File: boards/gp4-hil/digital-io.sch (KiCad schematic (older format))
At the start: 15 parts, among them Q1 SSM6N58NU, U15 TS3A4751, U16 TS3A4751, U17 TS3A4751, U18 TS3A4751, U19 TS3A4751, U2 XC7A100T-1FTG256C

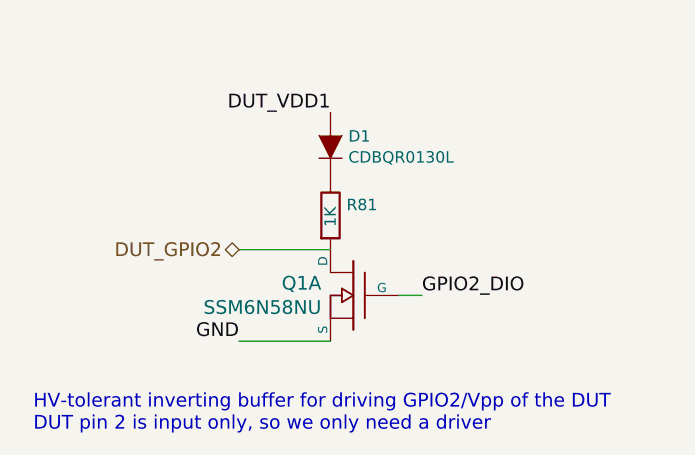
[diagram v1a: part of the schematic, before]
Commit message: Continued work on test board. Finally hooked up remote sense for 1V0.
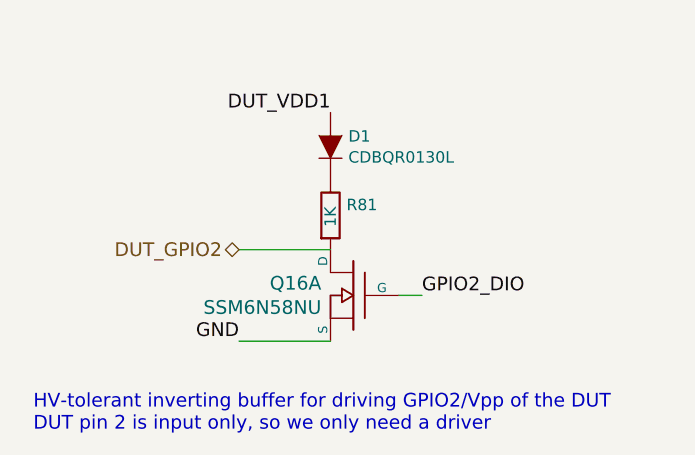
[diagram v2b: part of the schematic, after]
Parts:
- renumbered Q1 to Q16
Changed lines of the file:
@@
 Sheet 7 7
 Title "GreenPak Hardware-In-Loop Test Platform"
-Date "2016-06-05"
+Date "2016-06-10"
 Rev "0.1"
 Comp "Andrew Zonenberg"
@@
 HV-tolerant inverting buffer for driving GPIO2/Vpp of the DUT\nDUT pin 2 is input only, so we only need a driver
 $Comp
-L SSM6N58NU_DUAL_NMOS Q1
+L SSM6N58NU_DUAL_NMOS Q16
 U 1 1 573D1681
 P 2250 11150
-F 0 "Q1" H 2390 11203 60  0000 L CNN
+F 0 "Q16" H 2390 11203 60  0000 L CNN
 F 1 "SSM6N58NU" H 2390 11097 60  0000 L CNN
 F 2 "azonenberg_pcb:DFN_6_0.65MM_2x2MM_GDS" H 2250 11150 60  0001 C CNN

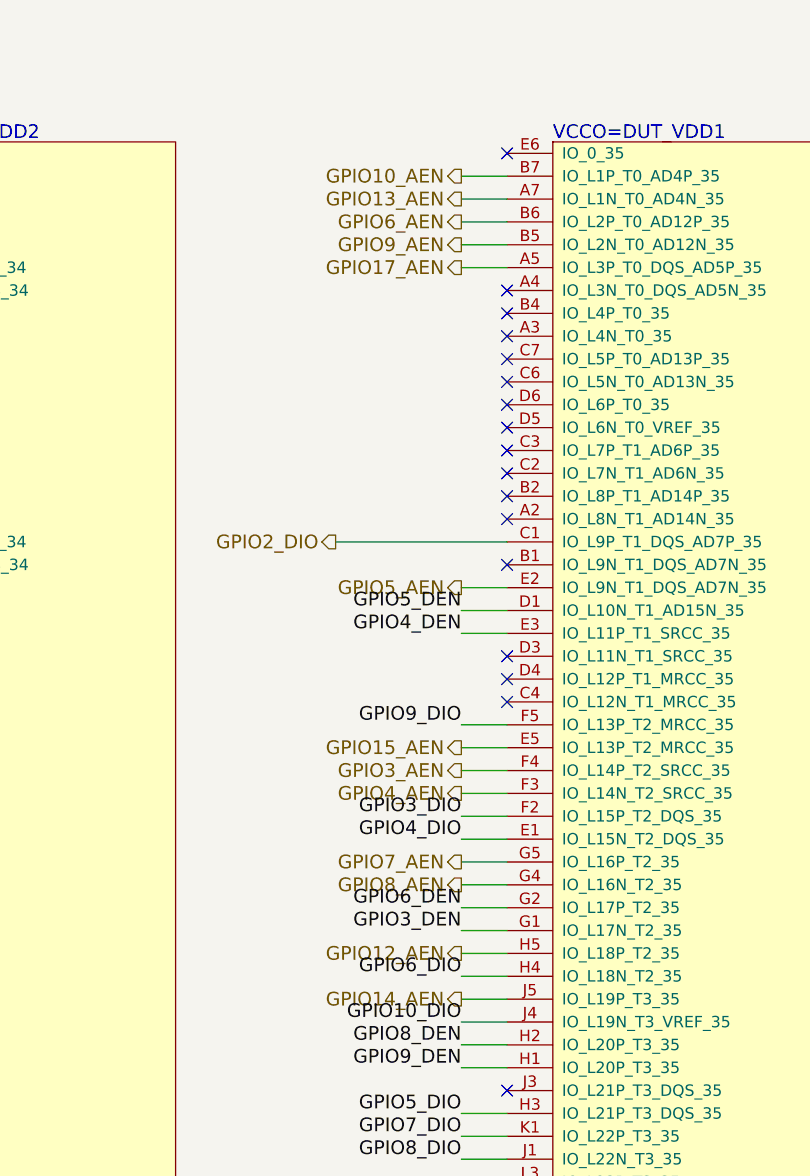
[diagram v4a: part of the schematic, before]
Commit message: Continued routing, began DAC stuff
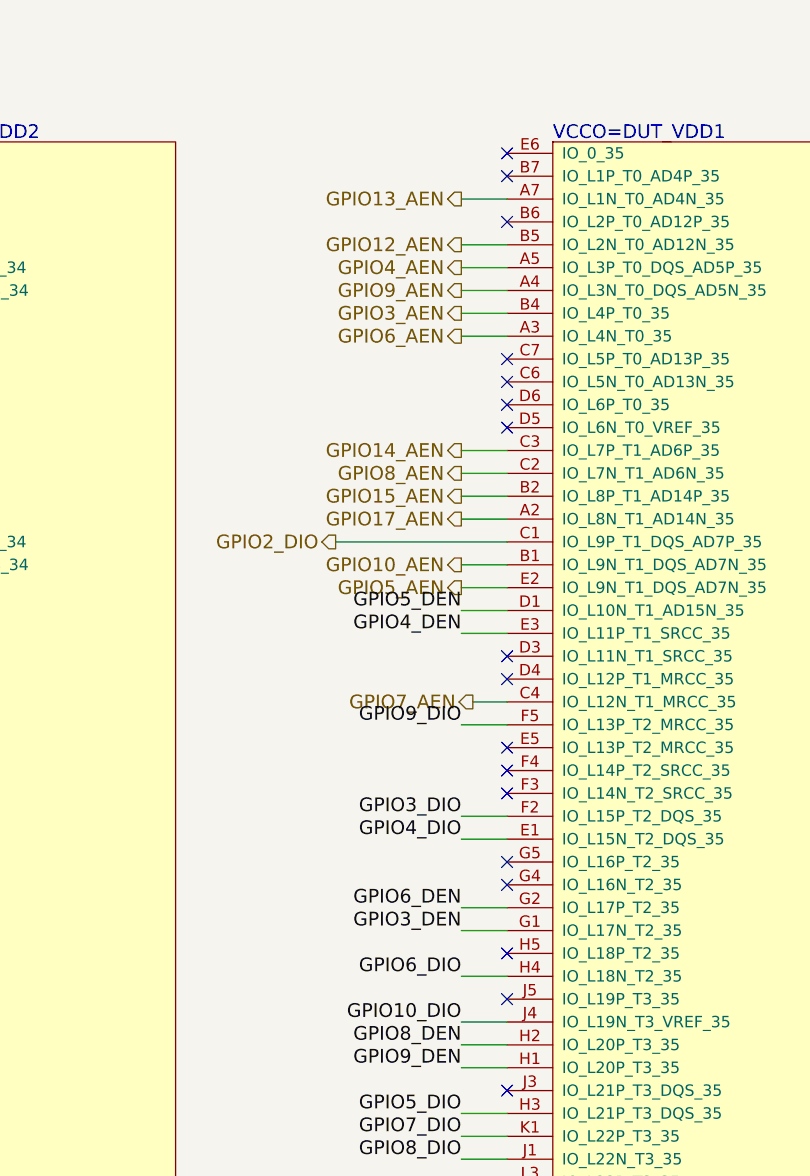
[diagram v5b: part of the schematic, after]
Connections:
- net GPIO10_AEN: now also U2.B1 (IO_L9N_T1_DQS_AD7N_35); no longer U2.B7 (IO_L1P_T0_AD4P_35)
- net GPIO12_AEN: now also U2.B5 (IO_L2N_T0_AD12N_35); no longer U2.H5 (IO_L18P_T2_35)
- net GPIO14_AEN: now also U2.C3 (IO_L7P_T1_AD6P_35); no longer U2.J5 (IO_L19P_T3_35)
- net GPIO15_AEN: now also U2.B2 (IO_L8P_T1_AD14P_35); no longer U2.E5 (IO_L13P_T2_MRCC_35)
- net GPIO17_AEN: now also U2.A2 (IO_L8N_T1_AD14N_35); no longer U2.A5 (IO_L3P_T0_DQS_AD5P_35)
- net GPIO3_AEN: now also U2.B4 (IO_L4P_T0_35); no longer U2.F4 (IO_L14P_T2_SRCC_35)
- net GPIO4_AEN: now also U2.A5 (IO_L3P_T0_DQS_AD5P_35); no longer U2.F3 (IO_L14N_T2_SRCC_35)
- net GPIO6_AEN: now also U2.A3 (IO_L4N_T0_35); no longer U2.B6 (IO_L2P_T0_AD12P_35)
- net GPIO7_AEN: now also U2.C4 (IO_L12N_T1_MRCC_35); no longer U2.G5 (IO_L16P_T2_35)
- net GPIO8_AEN: now also U2.C2 (IO_L7N_T1_AD6N_35); no longer U2.G4 (IO_L16N_T2_35)
- net GPIO9_AEN: now also U2.A4 (IO_L3N_T0_DQS_AD5N_35); no longer U2.B5 (IO_L2N_T0_AD12N_35)
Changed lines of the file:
@@
 Sheet 7 7
 Title "GreenPak Hardware-In-Loop Test Platform"
-Date "2016-06-12"
+Date "2016-06-13"
 Rev "0.1"
 Comp "Andrew Zonenberg"
@@
 Text HLabel 1500 8800 0    60   BiDi ~ 0
 DUT_GPIO20
-$Comp
-L XC7AxT-xFTG256x U?
-U 6 1 573B2D61
-P 19350 7550
-AR Path="/57316B0C/573B2D61" Ref="U?"  Part="1"
-AR Path="/573AABB3/573B2D61" Ref="U2"  Part="6"
-F 0 "U2" H 19350 7350 60  0000 L CNN
-F 1 "XC7A100T-1FTG256C" H 19350 7450 60  0000 L CNN
-F 2 "azonenberg_pcb:BGA_256_17x17_FULLARRAY_1MM" H 19350 7550 60  0001 C CNN
-F 3 "" H 19350 7550 60  0000 C CNN
-	6    19350 7550
-	1    0    0    -1
-$EndComp
 $Comp
 L TS3A4751 U15
@@
 	16150 3550 16000 3550
 Wire Wire Line
-	19150 2750 18950 2750
+	19150 4450 18950 4450
 Wire Wire Line
 	18950 2850 19150 2850
 Wire Wire Line
-	19150 2950 18950 2950
-Wire Wire Line
-	18950 3050 19150 3050
-Wire Wire Line
-	19150 3150 18950 3150
+	19150 3450 18950 3450
+Wire Wire Line
+	18950 3250 19150 3250
+Wire Wire Line
+	19150 4250 18950 4250
 Wire Wire Line
 	18950 7050 19150 7050
@@
 	19150 5150 18950 5150
 Wire Wire Line
-	18950 5250 19150 5250
+	18950 4150 19150 4150
 Wire Wire Line
 	7500 1300 7700 1300
@@
 	1750 11350 2150 11350
 NoConn ~ 19150 2650
-Text HLabel 18950 5350 0    60   Output ~ 0
+Text HLabel 18950 3350 0    60   Output ~ 0
 GPIO3_AEN
-Text HLabel 18950 5450 0    60   Output ~ 0
+Text HLabel 18950 3150 0    60   Output ~ 0
 GPIO4_AEN
 Text HLabel 18950 4550 0    60   Output ~ 0
 GPIO5_AEN
-Text HLabel 18950 2950 0    60   Output ~ 0
+Text HLabel 18950 3450 0    60   Output ~ 0
 GPIO6_AEN
-Text HLabel 18950 5750 0    60   Output ~ 0
+Text HLabel 19000 5050 0    60   Output ~ 0
 GPIO7_AEN
-Text HLabel 18950 5850 0    60   Output ~ 0
+Text HLabel 18950 4050 0    60   Output ~ 0
 GPIO8_AEN
+Text HLabel 18950 3250 0    60   Output ~ 0
+GPIO9_AEN
+Text HLabel 18950 4450 0    60   Output ~ 0
+GPIO10_AEN
+Wire Wire Line
+	18950 3350 19150 3350
+Wire Wire Line
+	19150 3150 18950 3150
+Wire Wire Line
+	18950 5550 19150 5550
+Wire Wire Line
+	19150 5650 18950 5650
+Wire Wire Line
+	19150 4050 18950 4050
+Wire Wire Line
+	18950 5950 19150 5950
+Wire Wire Line
+	19150 6050 18950 6050
 Text HLabel 18950 3050 0    60   Output ~ 0
-GPIO9_AEN
-Text HLabel 18950 2750 0    60   Output ~ 0
-GPIO10_AEN
-Wire Wire Line
-	18950 5350 19150 5350
-Wire Wire Line
-	19150 5450 18950 5450
-Wire Wire Line
-	18950 5550 19150 5550
-Wire Wire Line
-	19150 5650 18950 5650
-Wire Wire Line
-	18950 5750 19150 5750
-Wire Wire Line
-	19150 5850 18950 5850
-Wire Wire Line
-	18950 5950 19150 5950
-Wire Wire Line
-	19150 6050 18950 6050
-Text HLabel 18950 6150 0    60   Output ~ 0
 GPIO12_AEN
 Text HLabel 18950 2850 0    60   Output ~ 0
 GPIO13_AEN
-Text HLabel 18950 6350 0    60   Output ~ 0
+Text HLabel 18950 3950 0    60   Output ~ 0
 GPIO14_AEN
-Text HLabel 18950 5250 0    60   Output ~ 0
+Text HLabel 18950 4150 0    60   Output ~ 0
 GPIO15_AEN
-Text HLabel 18950 3150 0    60   Output ~ 0
+Text HLabel 18950 4250 0    60   Output ~ 0
 GPIO17_AEN
 Wire Wire Line
-	19150 6150 18950 6150
+	19150 3050 18950 3050
 Wire Wire Line
 	18950 6250 19150 6250
 Wire Wire Line
-	19150 6350 18950 6350
+	19150 3950 18950 3950
 Wire Wire Line
 	18950 6450 19150 6450
@@
 NoConn ~ 19150 3750
 NoConn ~ 19150 3850
-NoConn ~ 19150 3950
-NoConn ~ 19150 4050
-NoConn ~ 19150 4150
-NoConn ~ 19150 4250
 $Comp
 L XC7AxT-xFTG256x U?
@@
 Wire Wire Line
 	19150 7250 18950 7250
-NoConn ~ 19150 3450
 NoConn ~ 19150 4950
-NoConn ~ 19150 5050
-NoConn ~ 19150 3250
 NoConn ~ 19150 4850
-NoConn ~ 19150 3350
-NoConn ~ 19150 4450
+NoConn ~ 19150 2950
+$Comp
+L XC7AxT-xFTG256x U?
+U 6 1 573B2D61
+P 19350 7550
+AR Path="/57316B0C/573B2D61" Ref="U?"  Part="1"
+AR Path="/573AABB3/573B2D61" Ref="U2"  Part="6"
+F 0 "U2" H 19350 7350 60  0000 L CNN
+F 1 "XC7A100T-1FTG256C" H 19350 7450 60  0000 L CNN
+F 2 "azonenberg_pcb:BGA_256_17x17_FULLARRAY_1MM" H 19350 7550 60  0001 C CNN
+F 3 "" H 19350 7550 60  0000 C CNN
+	6    19350 7550
+	1    0    0    -1
+$EndComp
+NoConn ~ 19150 5250
+NoConn ~ 19150 5350
+NoConn ~ 19150 5750
+NoConn ~ 19150 5850
+NoConn ~ 19150 6150
+NoConn ~ 19150 6350
+NoConn ~ 19150 5450
+Wire Wire Line
+	19150 5050 19000 5050
+NoConn ~ 19150 2750
 $EndSCHEMATC
